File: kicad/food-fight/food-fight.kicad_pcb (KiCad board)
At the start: 2 copper layers, 315 x 257 mm, 28 parts, among them U10C 7406, U10M 74LS161, U10N 74LS161, U1F 74LS86, U1H 7407, U2C 74S08, U2D 74S157, U2H 74LS74, U2K 74LS74, U3A 74LS157, U3B 74LS157, U3P 74LS157, U4C 74LS86, U4F 74LS273, U4K 74LS367, U4L 74LS157, U4M 74LS157, U4N 74LS157, U4P 74S00, U5M 74LS194, U5N 74LS194, U6B 74LS273, U6H 74LS157, U6K 74LS273, U7M 74LS273, U8H 74LS245, U8M 74LS244, U8N 74LS244

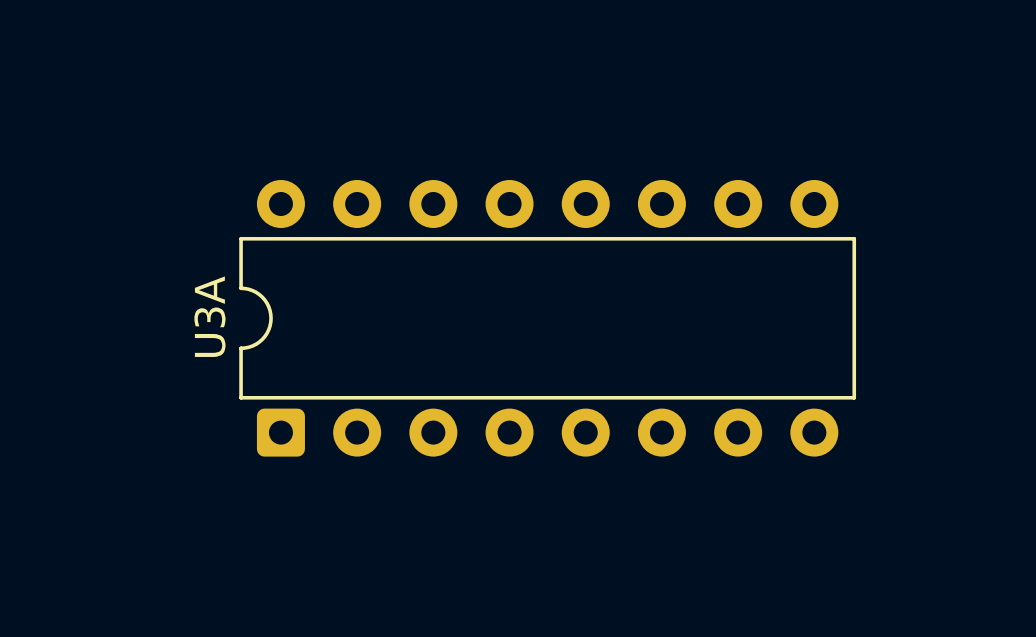
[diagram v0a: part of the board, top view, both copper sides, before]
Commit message: Drop a cell both readings claim, instead of taking the last one
locations() detects a designator claimed twice by the same parts list and
returns the collision alongside the mapping. harvest() took only
locations(...)[0] and dropped that half of the answer on the floor, so a
contested cell was resolved by whichever reading came last in the file.

22 devices on the published site were chosen that way: Food Fight 1, I-Robot 8,
Indy 4 3, Monte Carlo 4, Pole Position 6. They are withdrawn. merge only ever
adds cells, so re-running it could not undo them — they had to come off
explicitly. Both readings are recorded in each board's read file rather than
just deleted, because a repairer at the bench is better served by "it is one of
these two" than by a silent gap.

A contested cell is now kept only when every reading of it names the same
device — '74L886' against '74LS86' is one part and an OCR of S as 8, and Orbit's
three such cells stay. Anything else is dropped and printed.

It deliberately does NOT use plausible() to break the tie, though the
cross-printing split does. plausible() does not recognise the Fairchild 93xx and
96xx series: it calls 9312, 9322 and 9602 implausible, and 9316 too — which this
repo's own equivalence table documents as Fairchild's 74161. Filtering on it here
would have discarded the 9312 reading of Indy 4's B3 and "resolved" that cell to
a 7474, a different device entirely. A false correction is worse than the
collision it replaces. The split path has the same blind spot and is now flagged
in HANDOFF, unaudited.

The fix also unblocks the two boards withheld last time for exactly this reason.
Pole Position II (38 devices, 8 cells dropped) and Xevious (18, 1 dropped) no
longer need figure-splitting to be safe, because a cell nothing can attribute is
now simply absent rather than guessed.

47 boards, 2,489 devices.

Co-Authored-By: Claude Opus 5 <noreply@anthropic.com>
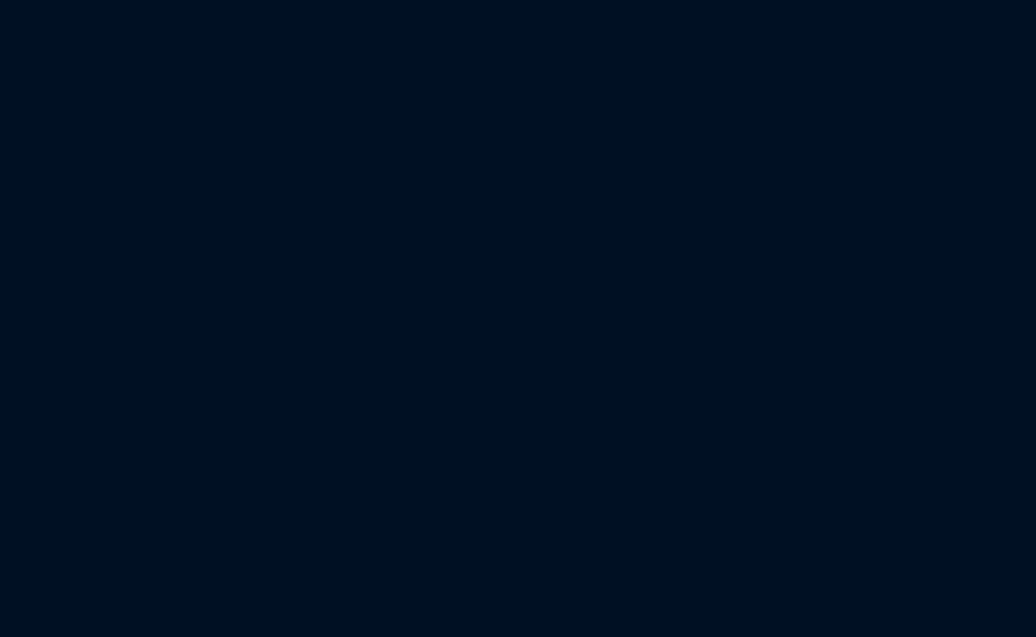
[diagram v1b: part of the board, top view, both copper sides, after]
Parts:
- removed U3A: 74LS157, DIP-16_W7.62mm

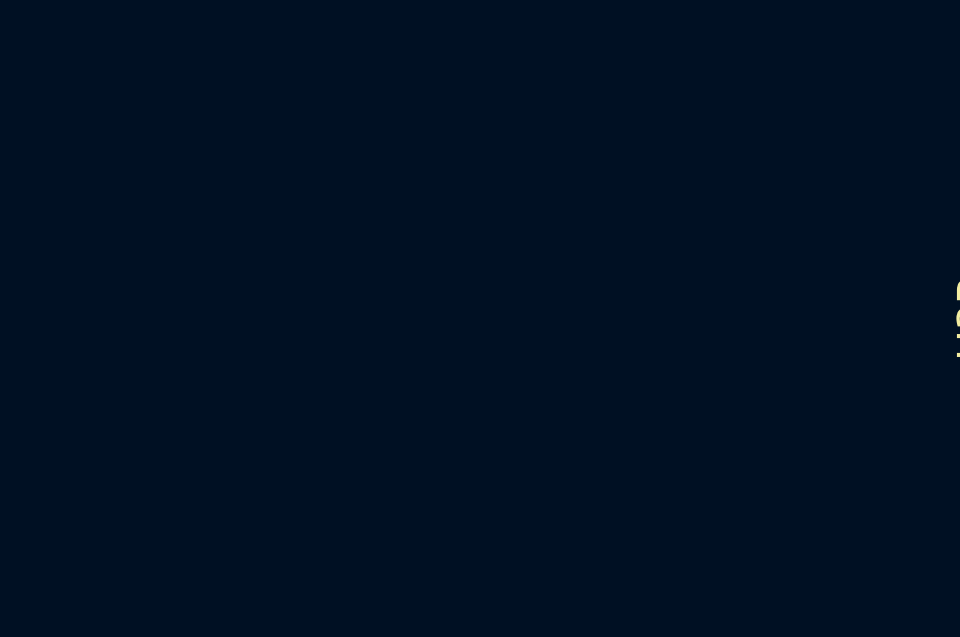
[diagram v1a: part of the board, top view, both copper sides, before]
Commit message: Teach plausible() the Fairchild parts; audit what it had decided
The last commit flagged that plausible() does not recognise the Fairchild
93xx/96xx series and left it unaudited. Audited now.

plausible() called 9312, 9316, 9321, 9322, 9300, 9301, 9334 and 9602
implausible — eight parts in 111 trusted rows and on 64 devices of published
maps, every one of them admitted by well_formed(). The two functions disagreed
about real parts, and 9316 is one this repo's own equivalence table documents
as Fairchild's 74161. Bounded to 9[36]\d{2}: a bare 9\d{3} would admit any
four-digit OCR smear.

The audit replayed the cross-printing split over every published board. 8 cells
had been decided by the filter. 4 were Asteroids P9, where a printing reading
9316 lost to one reading 74LS164 — the blind spot, discarding the more specific
reading as wreckage — and P9 is on none of the four Asteroids maps. The other 4
were the filter doing its job: 8728 to 8T28 on Football, 74LSI91 to 74LS191 on
Major Havoc, capital-I read as 1. After the fix 4 remain, all of the second
kind. No published device ever came from a false resolution.

Dropping a contested cell frees the readings a collision used to consume, so a
re-merge recovers 9 devices: Monte Carlo 3, Pole Position 4, Food Fight 1,
Soccer 1. Checked first that none of the 22 cells withdrawn last commit would
come back — every one is still reported as contested.

APB exposed a separate fault. Its 3B/F span names rows five apart, build_board
raised on it, and removing it by hand did not stick because the next merge wrote
it again — the adjacency rule lived only at build time, after the board file was
already wrong. It now runs where the designator is first accepted, and says so:
"impossible span 3B/F — those rows are not adjacent on this grid".

All 47 boards build. 2,498 devices.

Co-Authored-By: Claude Opus 5 <noreply@anthropic.com>
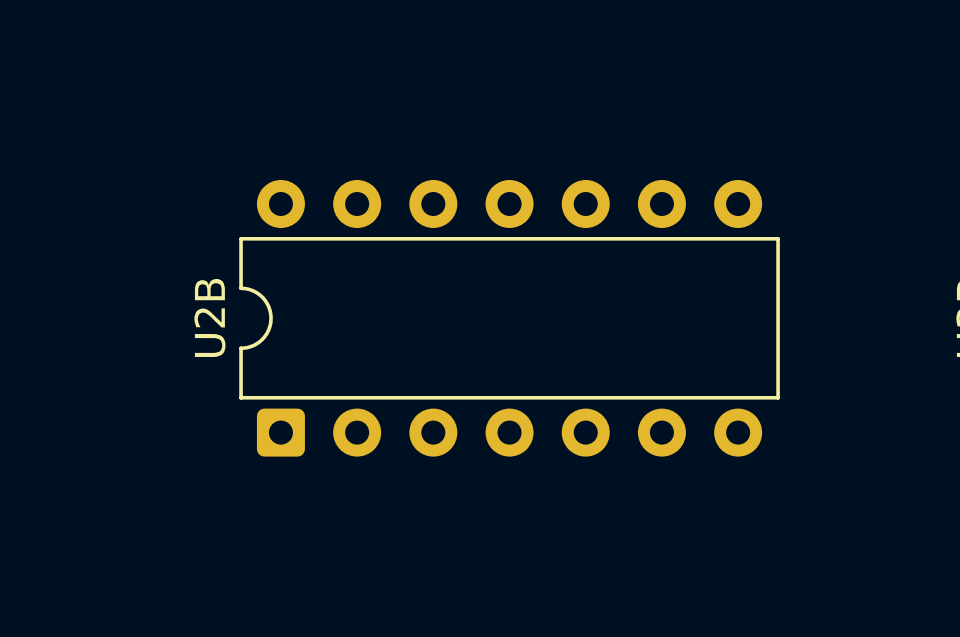
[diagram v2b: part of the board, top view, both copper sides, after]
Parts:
- added U2B: 74LS02, DIP-14_W7.62mm, F.Cu at (51.4, 208.5)
